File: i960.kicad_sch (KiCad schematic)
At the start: 50 parts

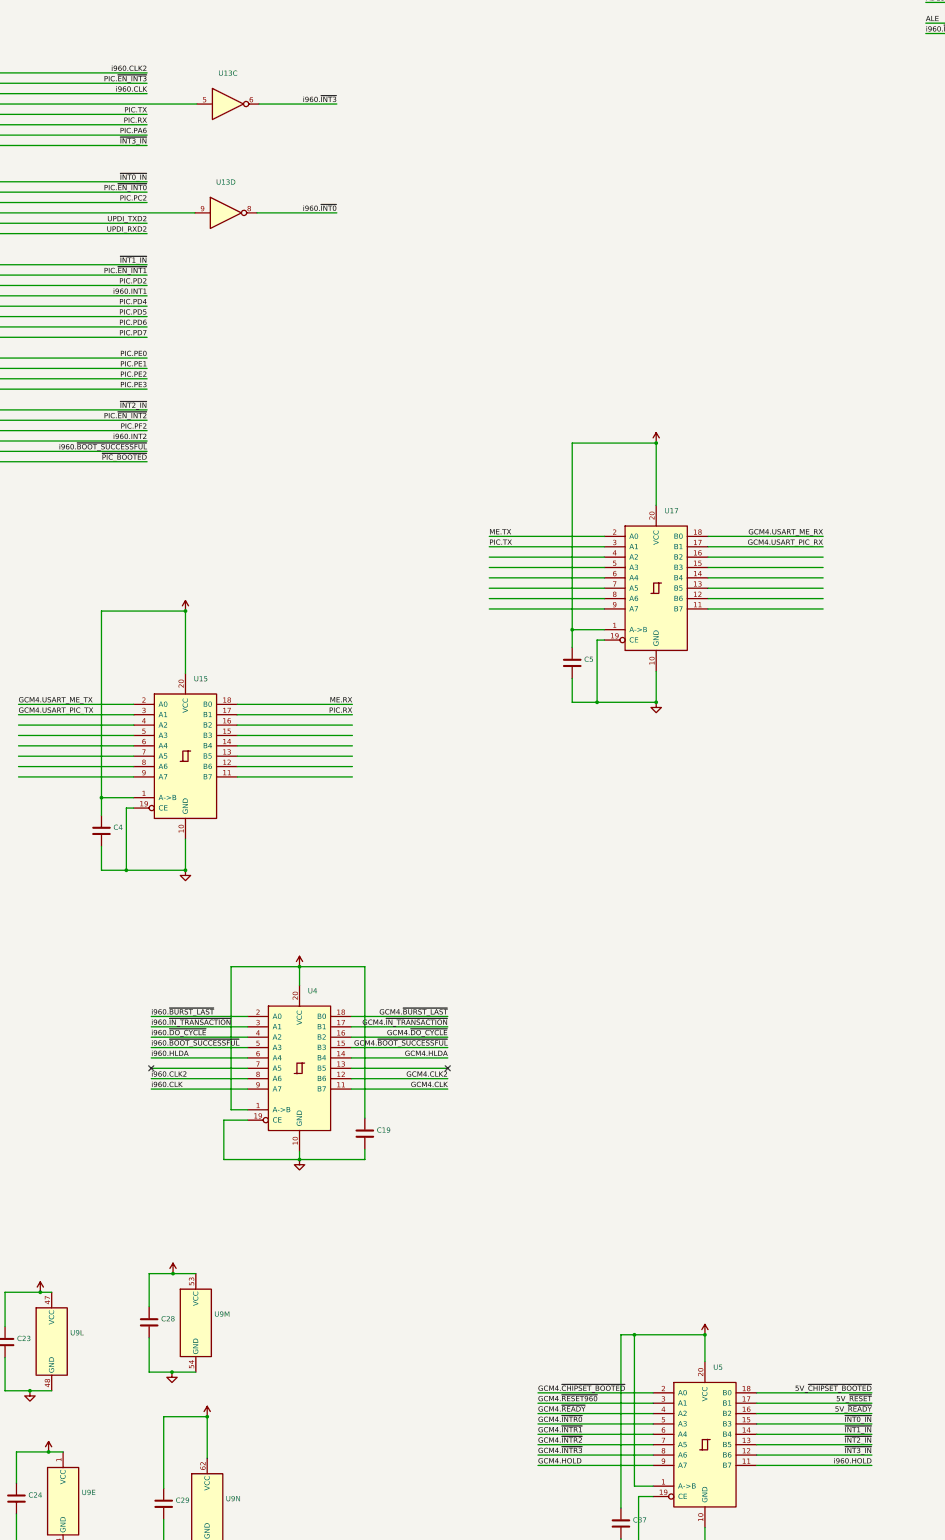
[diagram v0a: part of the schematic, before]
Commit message: Chipset only gets access to ~INT3 by default
Use the other interrupts for peripherals on the PIC.
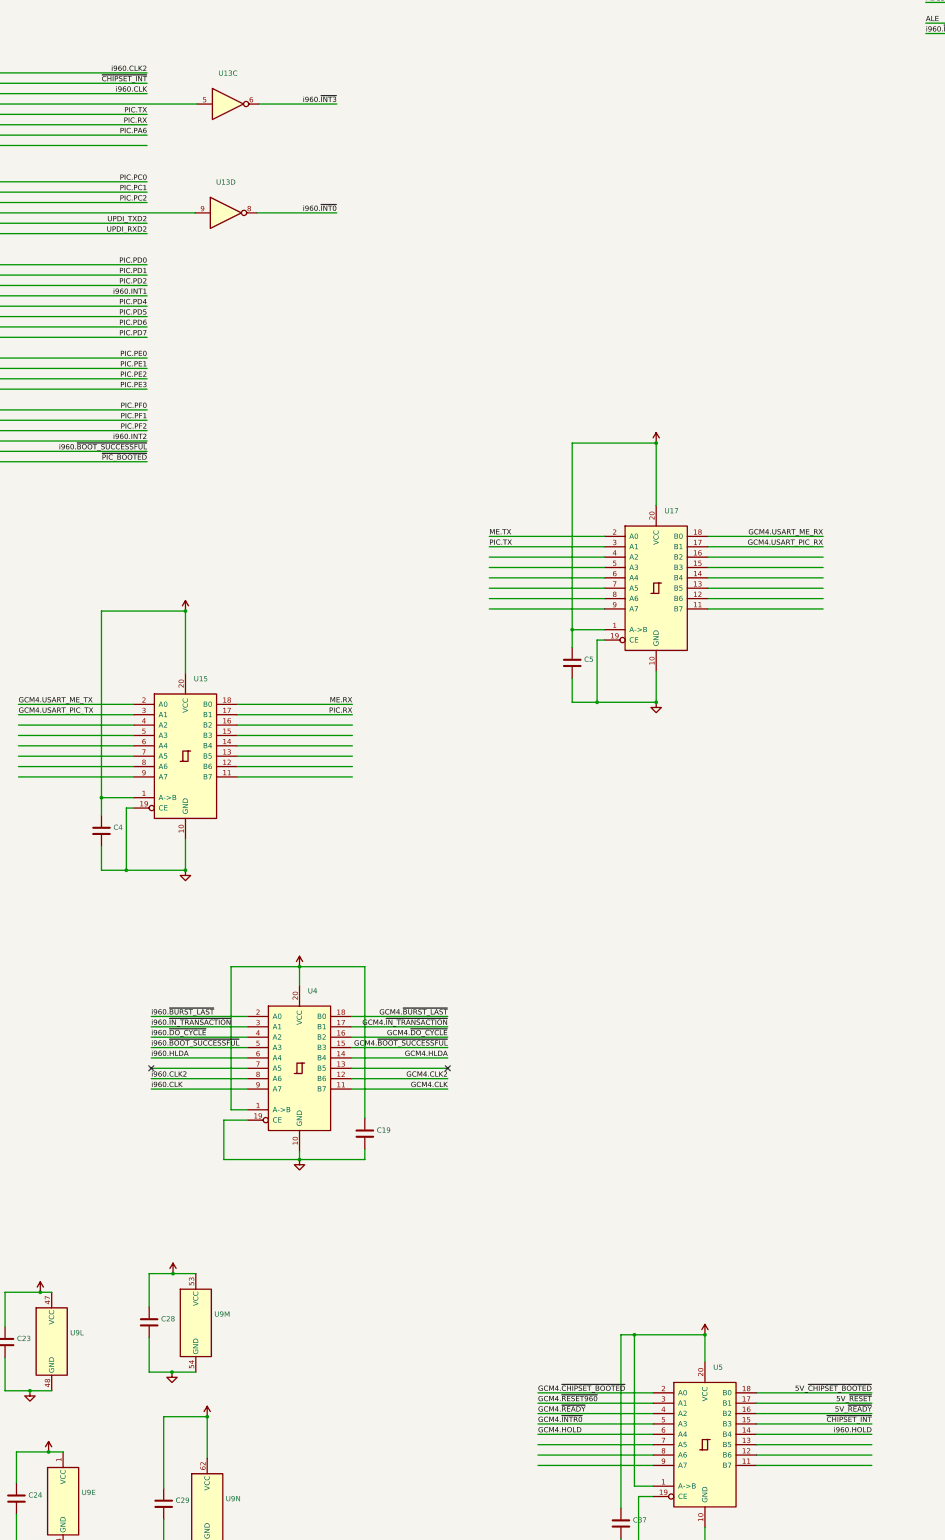
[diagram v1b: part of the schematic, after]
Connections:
- net GCM4.~{INTR1} is gone; now on net GCM4.HOLD: U5.6 (A4)
- net GCM4.HOLD: no longer U5.9 (A7)
- net i960.HOLD: now also U5.14 (B4); no longer U5.11 (B7)
- net GCM4.~{INTR2}: no longer names the net of U5.7 (A5)
- net GCM4.~{INTR3}: no longer names the net of U5.8 (A6)
- net PIC.~{EN_INT0} renamed PIC.PC1
- net PIC.~{EN_INT1} renamed PIC.PD1
- net PIC.~{EN_INT2} renamed PIC.PF1
- net PIC.~{EN_INT3} renamed ~{CHIPSET_INT}
- net ~{CHIPSET_INT}: now also U5.15 (B3)
- net ~{INT0_IN} renamed PIC.PC0
- net PIC.PC0: no longer U5.15 (B3)
- net ~{INT1_IN} renamed PIC.PD0
- net PIC.PD0: no longer U5.14 (B4)
- net ~{INT2_IN}: no longer names the net of U5.13 (B5)
- net ~{INT2_IN}: no longer U14.23 ((TOSC1/TXD2/CCL3-IN0)PF0)
- net ~{INT3_IN}: no longer names the net of U5.12 (B6)
- net ~{INT3_IN}: no longer U14.40 ((XDIR0_ALT/CLKO/~{SS})PA7)
- new net PIC.PF0: U14.23 ((TOSC1/TXD2/CCL3-IN0)PF0)
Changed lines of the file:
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@@
     (company "Joshua Scoggins")
   )
+  (bus_alias "ADR960" (members "A[0..31]" "D[0..15]" "BURST_A[1..3]" "~{DEN}" "DT\\~{R}" "W\\~{R}" "~{BE[0..1]}" "~{DATA_LINE_EN}" "CLK2" "CLK"))
   (bus_alias "CHIPSET" (members "~{BURST_LAST}" "~{IN_TRANSACTION}" "~{DO_CYCLE}" "~{BOOT_SUCCESSFUL}" "HLDA" "HOLD" "~{CHIPSET_BOOTED}" "~{RESET960}" "~{READY}" "~{INTR[0..3]}" "CLK2" "CLK" "L[0..15]" "A[0..1]" "~{EN}" "~{DEV_EN[0..3]}" "USART_ME_TX" "USART_ME_RX" "USART_PIC_TX" "USART_PIC_RX"))
-  (bus_alias "ADR960" (members "A[0..31]" "D[0..15]" "BURST_A[1..3]" "~{DEN}" "DT\\~{R}" "W\\~{R}" "~{BE[0..1]}" "~{DATA_LINE_EN}" "CLK2" "CLK"))
   (junction (at 299.974 362.966) (diameter 0) (color 0 0 0 0)
   )
@@
     (effects (font (size 1.27 1.27)) (justify left bottom))
   )
-  (label "GCM4.~{INTR1}" (at 285.496 542.29 0)
-    (effects (font (size 1.27 1.27)) (justify left bottom))
-  )
   (label "AD4" (at 442.976 112.014 0)
     (effects (font (size 1.27 1.27)) (justify left bottom))
@@
     (effects (font (size 1.27 1.27)) (justify left bottom))
   )
-  (label "~{INT2_IN}" (at 367.284 544.83 180)
-    (effects (font (size 1.27 1.27)) (justify right bottom))
-  )
   (label "i960.CLK2" (at 307.848 107.442 180)
     (effects (font (size 1.27 1.27)) (justify right bottom))
@@
     (effects (font (size 1.27 1.27)) (justify right bottom))
   )
-  (label "~{INT1_IN}" (at 189.738 255.778 180)
-    (effects (font (size 1.27 1.27)) (justify right bottom))
-  )
-  (label "GCM4.~{INTR2}" (at 285.496 544.83 0)
-    (effects (font (size 1.27 1.27)) (justify left bottom))
-  )
   (label "PIC.RX" (at 189.738 221.488 180)
     (effects (font (size 1.27 1.27)) (justify right bottom))
@@
     (effects (font (size 1.27 1.27)) (justify right bottom))
   )
-  (label "~{INT1_IN}" (at 367.284 542.29 180)
-    (effects (font (size 1.27 1.27)) (justify right bottom))
-  )
   (label "i960.~{IN_TRANSACTION}" (at 142.494 114.808 180)
     (effects (font (size 1.27 1.27)) (justify right bottom))
@@
     (effects (font (size 1.27 1.27)) (justify right bottom))
   )
-  (label "i960.HOLD" (at 367.284 549.91 180)
+  (label "i960.HOLD" (at 367.284 542.29 180)
     (effects (font (size 1.27 1.27)) (justify right bottom))
   )
@@
     (effects (font (size 1.27 1.27)) (justify right bottom))
   )
-  (label "~{INT2_IN}" (at 189.738 291.338 180)
-    (effects (font (size 1.27 1.27)) (justify right bottom))
-  )
   (label "PU3" (at 255.016 64.262 90)
     (effects (font (size 1.27 1.27)) (justify left bottom))
@@
     (effects (font (size 1.27 1.27)) (justify right bottom))
   )
-  (label "PIC.~{EN_INT3}" (at 189.738 211.328 180)
-    (effects (font (size 1.27 1.27)) (justify right bottom))
-  )
   (label "i960.~{BLAST}" (at 142.494 74.168 180)
     (effects (font (size 1.27 1.27)) (justify right bottom))
@@
     (effects (font (size 1.27 1.27)) (justify right bottom))
   )
-  (label "PIC.~{EN_INT2}" (at 189.738 293.878 180)
-    (effects (font (size 1.27 1.27)) (justify right bottom))
-  )
-  (label "~{INT0_IN}" (at 189.738 235.458 180)
-    (effects (font (size 1.27 1.27)) (justify right bottom))
-  )
   (label "GCM4.~{DO_CYCLE}" (at 263.3637 445.008 180)
     (effects (font (size 1.27 1.27)) (justify right bottom))
@@
     (effects (font (size 1.27 1.27)) (justify right bottom))
   )
-  (label "PIC.~{EN_INT0}" (at 189.738 237.998 180)
-    (effects (font (size 1.27 1.27)) (justify right bottom))
-  )
   (label "AD13" (at 442.976 134.874 0)
     (effects (font (size 1.27 1.27)) (justify left bottom))
@@
     (effects (font (size 1.27 1.27)) (justify left bottom))
   )
+  (label "PIC.PD1" (at 189.738 258.318 180)
+    (effects (font (size 1.27 1.27)) (justify right bottom))
+  )
   (label "GCM4.L14" (at 477.52 188.976 180)
     (effects (font (size 1.27 1.27)) (justify right bottom))
@@
     (effects (font (size 1.27 1.27)) (justify left bottom))
   )
-  (label "PIC.~{EN_INT1}" (at 189.738 258.318 180)
-    (effects (font (size 1.27 1.27)) (justify right bottom))
-  )
   (label "5V_~{RESET}" (at 20.066 64.008 0)
     (effects (font (size 1.27 1.27)) (justify left bottom))
@@
     (effects (font (size 1.27 1.27)) (justify left bottom))
   )
+  (label "PIC.PF0" (at 189.738 291.338 180)
+    (effects (font (size 1.27 1.27)) (justify right bottom))
+  )
   (label "i960.HLDA" (at 514.604 20.828 0)
     (effects (font (size 1.27 1.27)) (justify left bottom))
@@
     (effects (font (size 1.27 1.27)) (justify right bottom))
   )
-  (label "GCM4.HOLD" (at 285.496 549.91 0)
+  (label "GCM4.HOLD" (at 285.496 542.29 0)
     (effects (font (size 1.27 1.27)) (justify left bottom))
   )
@@
     (effects (font (size 1.27 1.27)) (justify right bottom))
   )
-  (label "GCM4.~{INTR3}" (at 285.496 547.37 0)
-    (effects (font (size 1.27 1.27)) (justify left bottom))
+  (label "PIC.PF1" (at 189.738 293.878 180)
+    (effects (font (size 1.27 1.27)) (justify right bottom))
   )
   (label "~{RESET960}" (at 199.136 132.588 180)
@@
     (effects (font (size 1.27 1.27)) (justify left bottom))
   )
+  (label "PIC.PC0" (at 189.738 235.458 180)
+    (effects (font (size 1.27 1.27)) (justify right bottom))
+  )
   (label "GCM4.L1" (at 553.974 271.526 180)
     (effects (font (size 1.27 1.27)) (justify right bottom))
@@
     (effects (font (size 1.27 1.27)) (justify left bottom))
   )
-  (label "~{INT3_IN}" (at 189.738 226.568 180)
+  (label "~{CHIPSET_INT}" (at 189.738 211.328 180)
     (effects (font (size 1.27 1.27)) (justify right bottom))
   )
@@
     (effects (font (size 1.27 1.27)) (justify right bottom))
   )
-  (label "~{INT3_IN}" (at 367.284 547.37 180)
-    (effects (font (size 1.27 1.27)) (justify right bottom))
-  )
   (label "i960.D4" (at 470.662 112.014 180)
     (effects (font (size 1.27 1.27)) (justify right bottom))
@@
     (effects (font (size 1.27 1.27)) (justify left bottom))
   )
+  (label "PIC.PD0" (at 189.738 255.778 180)
+    (effects (font (size 1.27 1.27)) (justify right bottom))
+  )
   (label "~{ME_READY}" (at 305.562 51.308 0)
     (effects (font (size 1.27 1.27)) (justify left bottom))
@@
     (effects (font (size 1.27 1.27)) (justify right bottom))
   )
-  (label "~{INT0_IN}" (at 367.284 539.75 180)
+  (label "~{CHIPSET_INT}" (at 367.284 539.75 180)
     (effects (font (size 1.27 1.27)) (justify right bottom))
   )
@@
     (effects (font (size 1.27 1.27)) (justify right bottom))
   )
+  (label "PIC.PC1" (at 189.738 237.998 180)
+    (effects (font (size 1.27 1.27)) (justify right bottom))
+  )
